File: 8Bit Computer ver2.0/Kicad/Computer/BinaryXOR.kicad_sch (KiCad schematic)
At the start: 4 parts, among them IC1 SN74ABT574ADWR, IC2 SN74AHC74DR, IC25 SN74AHC86DR, IC3 SN74LVC1G14DBVR

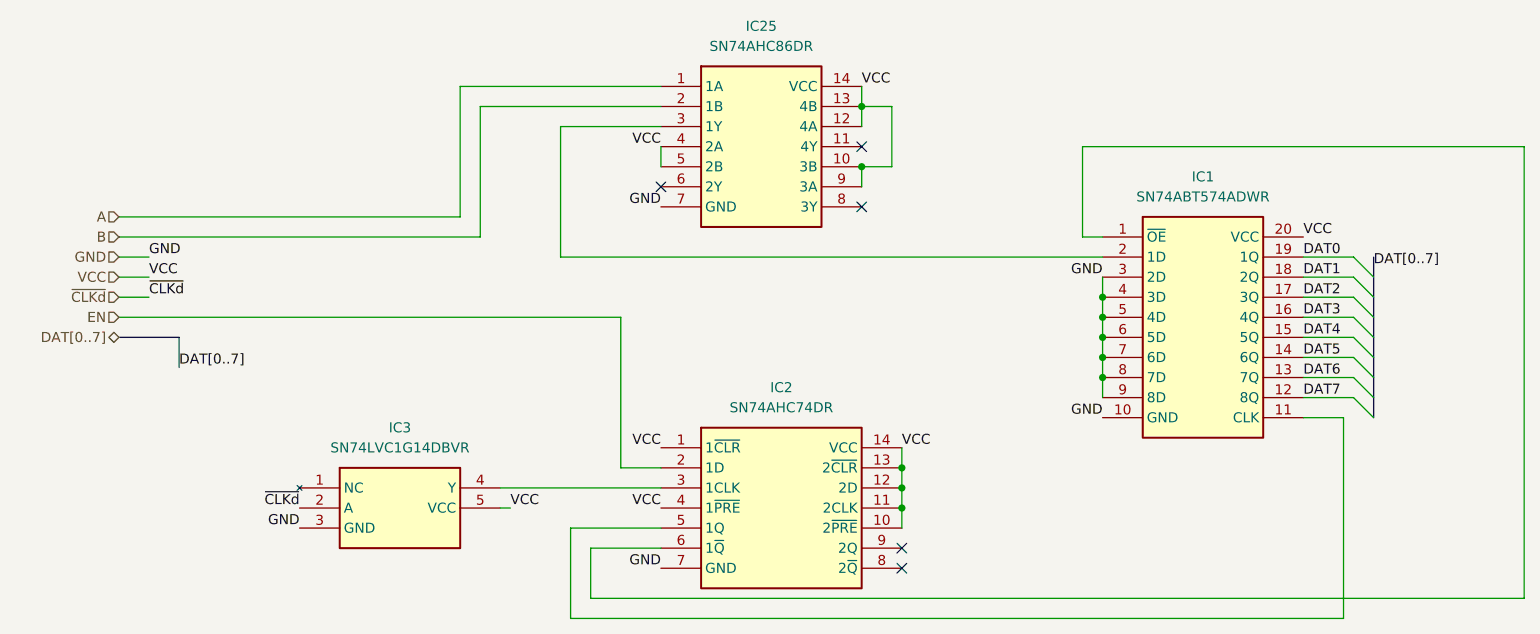
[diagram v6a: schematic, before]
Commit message: Kicad SCH/PCB
Kicad SCH/PCB:
changed the References in SCH
began with INOUTPUT module nearly done
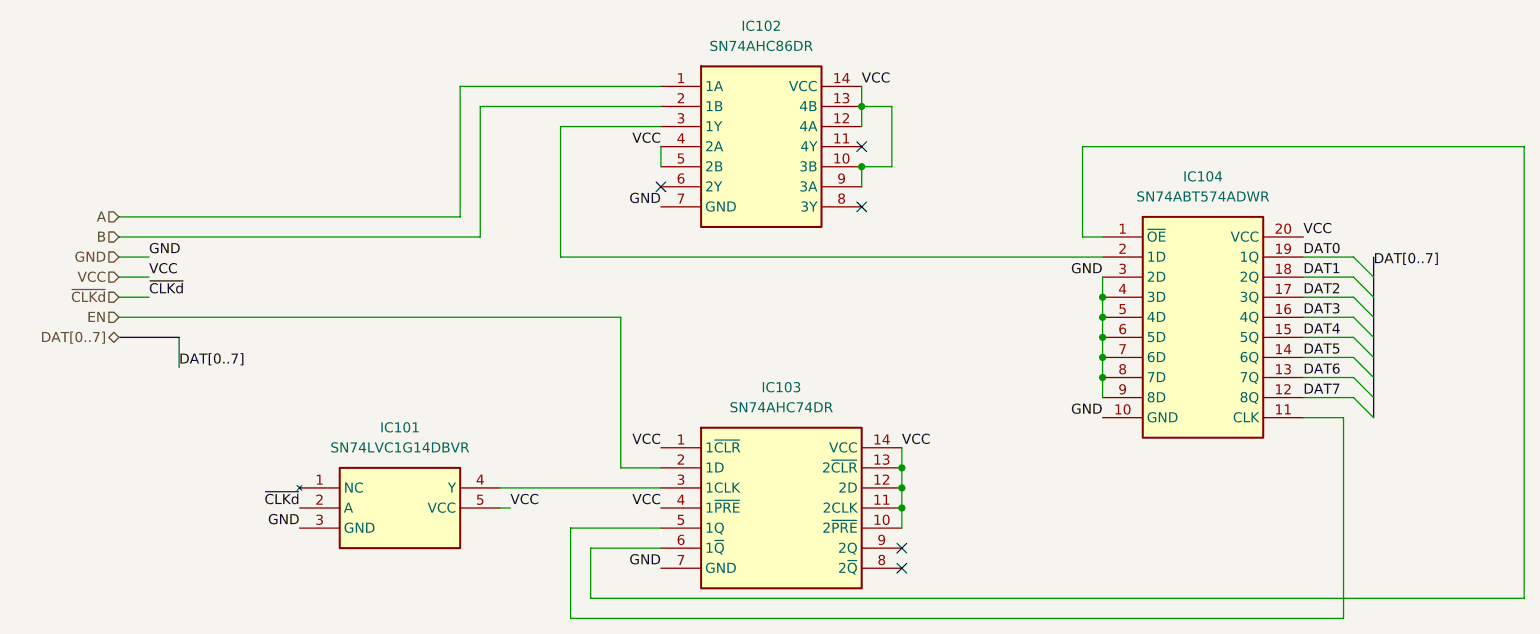
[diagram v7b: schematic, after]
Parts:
- renumbered IC3 to IC101, IC25 to IC102, IC2 to IC103, IC1 to IC104
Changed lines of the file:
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@@
 		(dnp no)
 		(fields_autoplaced yes)
-		(property "Reference" "IC25"
+		(property "Reference" "IC102"
 			(at 106.68 45.72 0)
 			(effects
@@
 			(project "Computer"
 				(path "/1196a00e-6878-4d6d-82b7-9e052dfe7c14/c4d8b530-1c6d-45af-88d2-7dc1d4321a34/4a21659e-6e4a-4683-bbd6-72ca2c7a4ec9"
-					(reference "IC25")
+					(reference "IC102")
 					(unit 1)
 				)
@@
 		(dnp no)
 		(fields_autoplaced yes)
-		(property "Reference" "IC3"
+		(property "Reference" "IC101"
 			(at 60.96 96.52 0)
 			(effects
@@
 			(project "Computer"
 				(path "/1196a00e-6878-4d6d-82b7-9e052dfe7c14/c4d8b530-1c6d-45af-88d2-7dc1d4321a34/4a21659e-6e4a-4683-bbd6-72ca2c7a4ec9"
-					(reference "IC3")
+					(reference "IC101")
 					(unit 1)
 				)
@@
 		(dnp no)
 		(fields_autoplaced yes)
-		(property "Reference" "IC2"
+		(property "Reference" "IC103"
 			(at 109.22 91.44 0)
 			(effects
@@
 			(project "Computer"
 				(path "/1196a00e-6878-4d6d-82b7-9e052dfe7c14/c4d8b530-1c6d-45af-88d2-7dc1d4321a34/4a21659e-6e4a-4683-bbd6-72ca2c7a4ec9"
-					(reference "IC2")
+					(reference "IC103")
 					(unit 1)
 				)
@@
 		(dnp no)
 		(fields_autoplaced yes)
-		(property "Reference" "IC1"
+		(property "Reference" "IC104"
 			(at 162.56 64.77 0)
 			(effects
@@
 			(project "Computer"
 				(path "/1196a00e-6878-4d6d-82b7-9e052dfe7c14/c4d8b530-1c6d-45af-88d2-7dc1d4321a34/4a21659e-6e4a-4683-bbd6-72ca2c7a4ec9"
-					(reference "IC1")
+					(reference "IC104")
 					(unit 1)
 				)

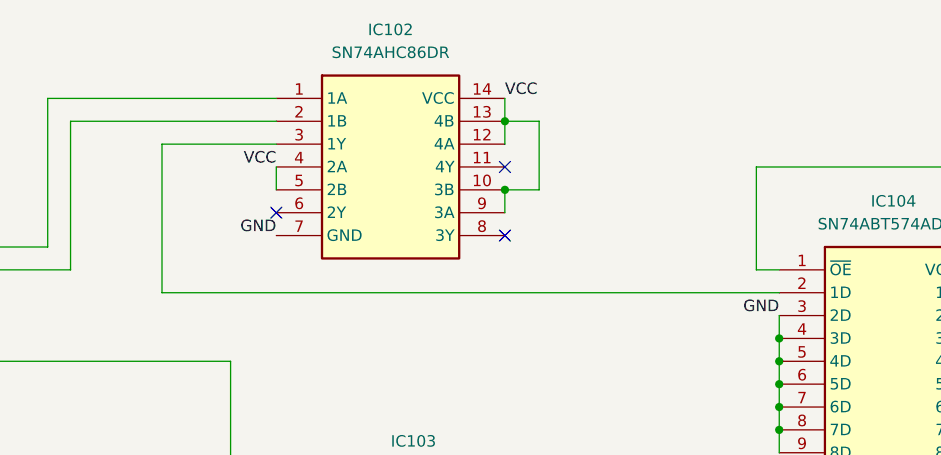
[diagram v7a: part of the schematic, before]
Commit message: Kicad
added 10pin 2,54mm Header
finished ALU PCB and added pin Header for extra use (DAT,ADR,CMD,Ddis,CLK)
31.12-06.01 about +60hr for ALU
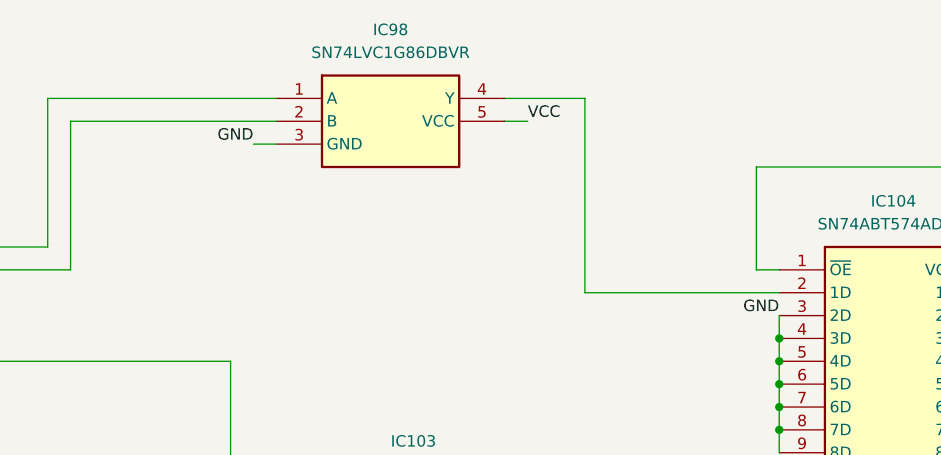
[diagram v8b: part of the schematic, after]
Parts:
- removed IC102: SN74AHC86DR, Samacsys:SOIC127P600X175-14N, symbol Samacsys:SN74AHC86DR
- added IC98: SN74LVC1G86DBVR, Samacsys:SOT95P280X145-5N, symbol Samacsys:SN74LVC1G86DBVR
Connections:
- net A: now also IC98.1 (A)
- net B: now also IC98.2 (B)
- net GND: now also IC98.3 (GND)
- net VCC: now also IC98.5 (VCC)
- net at IC104.2 (1D): now also IC98.4 (Y)
- no-connect marks 5 -> 2
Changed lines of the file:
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@@
-	)
-	(junction
-		(at 119.38 55.88)
-		(diameter 0)
-		(color 0 0 0 0)
 	)
 	(junction
@@
 	)
 	(junction
-		(at 119.38 63.5)
-		(diameter 0)
-		(color 0 0 0 0)
-	)
-	(junction
 		(at 149.86 85.09)
 		(diameter 0)
@@
 	)
 	(no_connect
-		(at 119.38 60.96)
-	)
-	(no_connect
-		(at 93.98 66.04)
-	)
-	(no_connect
-		(at 119.38 68.58)
-	)
-	(no_connect
 		(at 124.46 111.76)
 	)
@@
 	(wire
 		(pts
-			(xy 149.86 74.93) (xy 81.28 74.93)
-		)
-		(stroke
-			(width 0)
-			(type default)
-		)
-	)
-	(wire
-		(pts
-			(xy 119.38 53.34) (xy 119.38 55.88)
+			(xy 149.86 74.93) (xy 128.27 74.93)
 		)
 		(stroke
@@
 	(wire
 		(pts
+			(xy 91.44 58.42) (xy 93.98 58.42)
+		)
+		(stroke
+			(width 0)
+			(type default)
+		)
+	)
+	(wire
+		(pts
 			(xy 85.09 118.11) (xy 203.2 118.11)
 		)
@@
 	(wire
 		(pts
-			(xy 119.38 55.88) (xy 119.38 58.42)
-		)
-		(stroke
-			(width 0)
-			(type default)
-		)
-	)
-	(wire
-		(pts
 			(xy 175.26 85.09) (xy 181.61 85.09)
 		)
@@
 	(wire
 		(pts
-			(xy 119.38 63.5) (xy 119.38 66.04)
-		)
-		(stroke
-			(width 0)
-			(type default)
-		)
-	)
-	(wire
-		(pts
 			(xy 124.46 106.68) (xy 124.46 109.22)
 		)
@@
 	(wire
 		(pts
-			(xy 119.38 63.5) (xy 123.19 63.5)
-		)
-		(stroke
-			(width 0)
-			(type default)
-		)
-	)
-	(wire
-		(pts
 			(xy 203.2 118.11) (xy 203.2 60.96)
 		)
@@
 	(wire
 		(pts
-			(xy 123.19 55.88) (xy 119.38 55.88)
-		)
-		(stroke
-			(width 0)
-			(type default)
-		)
-	)
-	(wire
-		(pts
 			(xy 25.4 72.39) (xy 71.12 72.39)
 		)
@@
 	(wire
 		(pts
-			(xy 123.19 63.5) (xy 123.19 55.88)
+			(xy 119.38 55.88) (xy 121.92 55.88)
 		)
 		(stroke
@@
 		)
 	)
-	(wire
-		(pts
-			(xy 93.98 60.96) (xy 93.98 63.5)
-		)
-		(stroke
-			(width 0)
-			(type default)
-		)
-	)
 	(bus
 		(pts
@@
 	(wire
 		(pts
+			(xy 119.38 53.34) (xy 128.27 53.34)
+		)
+		(stroke
+			(width 0)
+			(type default)
+		)
+	)
+	(wire
+		(pts
 			(xy 93.98 111.76) (xy 85.09 111.76)
 		)
@@
 	(wire
 		(pts
-			(xy 81.28 74.93) (xy 81.28 58.42)
+			(xy 128.27 53.34) (xy 128.27 74.93)
 		)
 		(stroke
@@
 		(pts
 			(xy 184.15 87.63) (xy 184.15 90.17)
-		)
-		(stroke
-			(width 0)
-			(type default)
-		)
-	)
-	(wire
-		(pts
-			(xy 81.28 58.42) (xy 93.98 58.42)
 		)
 		(stroke
@@
 		)
 	)
-	(label "VCC"
-		(at 119.38 53.34 0)
-		(effects
-			(font
-				(size 1.27 1.27)
-			)
-			(justify left bottom)
-		)
-	)
 	(label "GND"
-		(at 93.98 68.58 180)
+		(at 91.44 58.42 180)
 		(effects
 			(font
@@
 	)
 	(label "VCC"
-		(at 93.98 60.96 180)
-		(effects
-			(font
-				(size 1.27 1.27)
-			)
-			(justify right bottom)
+		(at 121.92 55.88 0)
+		(effects
+			(font
+				(size 1.27 1.27)
+			)
+			(justify left bottom)
 		)
 	)
@@
 			)
 			(justify right)
-		)
-	)
-	(symbol
-		(lib_id "Samacsys:SN74AHC86DR")
-		(at 93.98 53.34 0)
-		(unit 1)
-		(exclude_from_sim no)
-		(in_bom yes)
-		(on_board yes)
-		(dnp no)
-		(fields_autoplaced yes)
-		(property "Reference" "IC102"
-			(at 106.68 45.72 0)
-			(effects
-				(font
-					(size 1.27 1.27)
-				)
-			)
-		)
-		(property "Value" "SN74AHC86DR"
-			(at 106.68 48.26 0)
-			(effects
-				(font
-					(size 1.27 1.27)
-				)
-			)
-		)
-		(property "Footprint" "Samacsys:SOIC127P600X175-14N"
-			(at 115.57 148.26 0)
-			(effects
-				(font
-					(size 1.27 1.27)
-				)
-				(justify left top)
-				(hide yes)
-			)
-		)
-		(property "Datasheet" "http://www.ti.com/lit/gpn/sn74ahc86"
-			(at 115.57 248.26 0)
-			(effects
-				(font
-					(size 1.27 1.27)
-				)
-				(justify left top)
-				(hide yes)
-			)
-		)
-		(property "Description" "Quadruple 2-Input Exclusive-OR Gates"
-			(at 93.98 53.34 0)
-			(effects
-				(font
-					(size 1.27 1.27)
-				)
-				(hide yes)
-			)
-		)
-		(property "Height" "1.75"
-			(at 115.57 448.26 0)
-			(effects
-				(font
-					(size 1.27 1.27)
-				)
-				(justify left top)
-				(hide yes)
-			)
-		)
-		(property "Mouser Part Number" "595-SN74AHC86DR"
-			(at 115.57 548.26 0)
-			(effects
-				(font
-					(size 1.27 1.27)
-				)
-				(justify left top)
-				(hide yes)
-			)
-		)
-		(property "Mouser Price/Stock" "https://www.mouser.co.uk/ProductDetail/Texas-Instruments/SN74AHC86DR?qs=D5pVkbrsqqK0yvWJ8LFETg%3D%3D"
-			(at 115.57 648.26 0)
-			(effects
-				(font
-					(size 1.27 1.27)
-				)
-				(justify left top)
-				(hide yes)
-			)
-		)
-		(property "Manufacturer_Name" "Texas Instruments"
-			(at 115.57 748.26 0)
-			(effects
-				(font
-					(size 1.27 1.27)
-				)
-				(justify left top)
-				(hide yes)
-			)
-		)
-		(property "Manufacturer_Part_Number" "SN74AHC86DR"
-			(at 115.57 848.26 0)
-			(effects
-				(font
-					(size 1.27 1.27)
-				)
-				(justify left top)
-				(hide yes)
-			)
-		)
-		(pin "13"
-		)
-		(pin "9"
-		)
-		(pin "11"
-		)
-		(pin "7"
-		)
-		(pin "14"
-		)
-		(pin "6"
-		)
-		(pin "12"
-		)
-		(pin "4"
-		)
-		(pin "10"
-		)
-		(pin "2"
-		)
-		(pin "3"
-		)
-		(pin "8"
-		)
-		(pin "5"
-		)
-		(pin "1"
-		)
-		(instances
-			(project "Computer"
-				(path "/1196a00e-6878-4d6d-82b7-9e052dfe7c14/c4d8b530-1c6d-45af-88d2-7dc1d4321a34/4a21659e-6e4a-4683-bbd6-72ca2c7a4ec9"
-					(reference "IC102")
-					(unit 1)
-				)
-			)
 		)
 	)
@@
 					(unit 1)
 				)
+			)
+		)
+	)
+	(symbol
+		(lib_id "Samacsys:SN74LVC1G86DBVR")
+		(at 93.98 53.34 0)
+		(unit 1)
+		(exclude_from_sim no)
+		(in_bom yes)
+		(on_board yes)
+		(dnp no)
+		(fields_autoplaced yes)
+		(property "Reference" "IC98"
+			(at 106.68 45.72 0)
+			(effects
+				(font
+					(size 1.27 1.27)
+				)
+			)
+		)
+		(property "Value" "SN74LVC1G86DBVR"
+			(at 106.68 48.26 0)
+			(effects
+				(font
+					(size 1.27 1.27)
+				)
+			)
+		)
+		(property "Footprint" "Samacsys:SOT95P280X145-5N"
+			(at 115.57 148.26 0)
+			(effects
+				(font
+					(size 1.27 1.27)
+				)
+				(justify left top)
+				(hide yes)
+			)
+		)
+		(property "Datasheet" "http://www.ti.com/lit/ds/symlink/sn74lvc1g86.pdf"
+			(at 115.57 248.26 0)
+			(effects
+				(font
+					(size 1.27 1.27)
+				)
+				(justify left top)
+				(hide yes)
+			)
+		)
+		(property "Description" "Single 2-Input Exclusive-OR Gate"
+			(at 93.98 53.34 0)
+			(effects
+				(font
+					(size 1.27 1.27)
+				)
+				(hide yes)
+			)
+		)
+		(property "Height" "1.45"
+			(at 115.57 448.26 0)
+			(effects
+				(font
+					(size 1.27 1.27)
+				)
+				(justify left top)
+				(hide yes)
+			)
+		)
+		(property "Mouser Part Number" "595-SN74LVC1G86DBVR"
+			(at 115.57 548.26 0)
+			(effects
+				(font
+					(size 1.27 1.27)
+				)
+				(justify left top)
+				(hide yes)
+			)
+		)
+		(property "Mouser Price/Stock" "https://www.mouser.co.uk/ProductDetail/Texas-Instruments/SN74LVC1G86DBVR?qs=d9gICRQKuCcyH%2F0J6yE9tQ%3D%3D"
+			(at 115.57 648.26 0)
+			(effects
+				(font
+					(size 1.27 1.27)
+				)
+				(justify left top)
+				(hide yes)
+			)
+		)
+		(property "Manufacturer_Name" "Texas Instruments"
+			(at 115.57 748.26 0)
+			(effects
+				(font
+					(size 1.27 1.27)
+				)
+				(justify left top)
+				(hide yes)
+			)
+		)
+		(property "Manufacturer_Part_Number" "SN74LVC1G86DBVR"
+			(at 115.57 848.26 0)
+			(effects
+				(font
+					(size 1.27 1.27)
+				)
+				(justify left top)
+				(hide yes)
+			)
+		)
+		(pin "5"
+		)
+		(pin "1"
+		)
+		(pin "2"
+		)
+		(pin "3"
+		)
+		(pin "4"
+		)
+		(instances
+			(project ""
+				(path "/1196a00e-6878-4d6d-82b7-9e052dfe7c14/c4d8b530-1c6d-45af-88d2-7dc1d4321a34/4a21659e-6e4a-4683-bbd6-72ca2c7a4ec9"
+					(reference "IC98")
+					(unit 1)
+				)
